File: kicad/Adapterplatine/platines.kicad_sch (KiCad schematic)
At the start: 6 parts, among them X28_1 Conn_01x05_Pin, X29_1 Conn_01x05_Pin, X46 Conn_02x05_Top_Bottom, X46__1 Conn_02x05_Top_Bottom, X48 Conn_02x10_Top_Bottom

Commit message: Bessere Verlegungen Adapterplatine
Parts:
- removed X46, X46__1: Conn_02x05_Top_Bottom, Connector_IDC:IDC-Header_2x05_P2.54mm_Vertical, symbol Connector_Generic:Conn_02x05_Top_Bottom
- added 230V_Platine1, X46: Conn_02x05_Odd_Even, Connector_IDC:IDC-Header_2x05_P2.54mm_Vertical, symbol Connector_Generic:Conn_02x05_Odd_Even
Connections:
- net +5V: now also 230V_Platine1.1 (Pin_1), X46.2 (Pin_2)
- net GND: now also 230V_Platine1.2 (Pin_2), X46.10 (Pin_10)
- new net: 230V_Platine1.10 (Pin_10), X46.1 (Pin_1)
- new net: 230V_Platine1.3 (Pin_3), X46.9 (Pin_9)
- new net: 230V_Platine1.4 (Pin_4), X46.8 (Pin_8)
- new net: 230V_Platine1.5 (Pin_5), X46.7 (Pin_7)
- new net: 230V_Platine1.6 (Pin_6), X46.6 (Pin_6)
- new net: 230V_Platine1.7 (Pin_7), X46.5 (Pin_5)
- new net: 230V_Platine1.8 (Pin_8), X46.4 (Pin_4)
- new net: 230V_Platine1.9 (Pin_9), X46.3 (Pin_3)

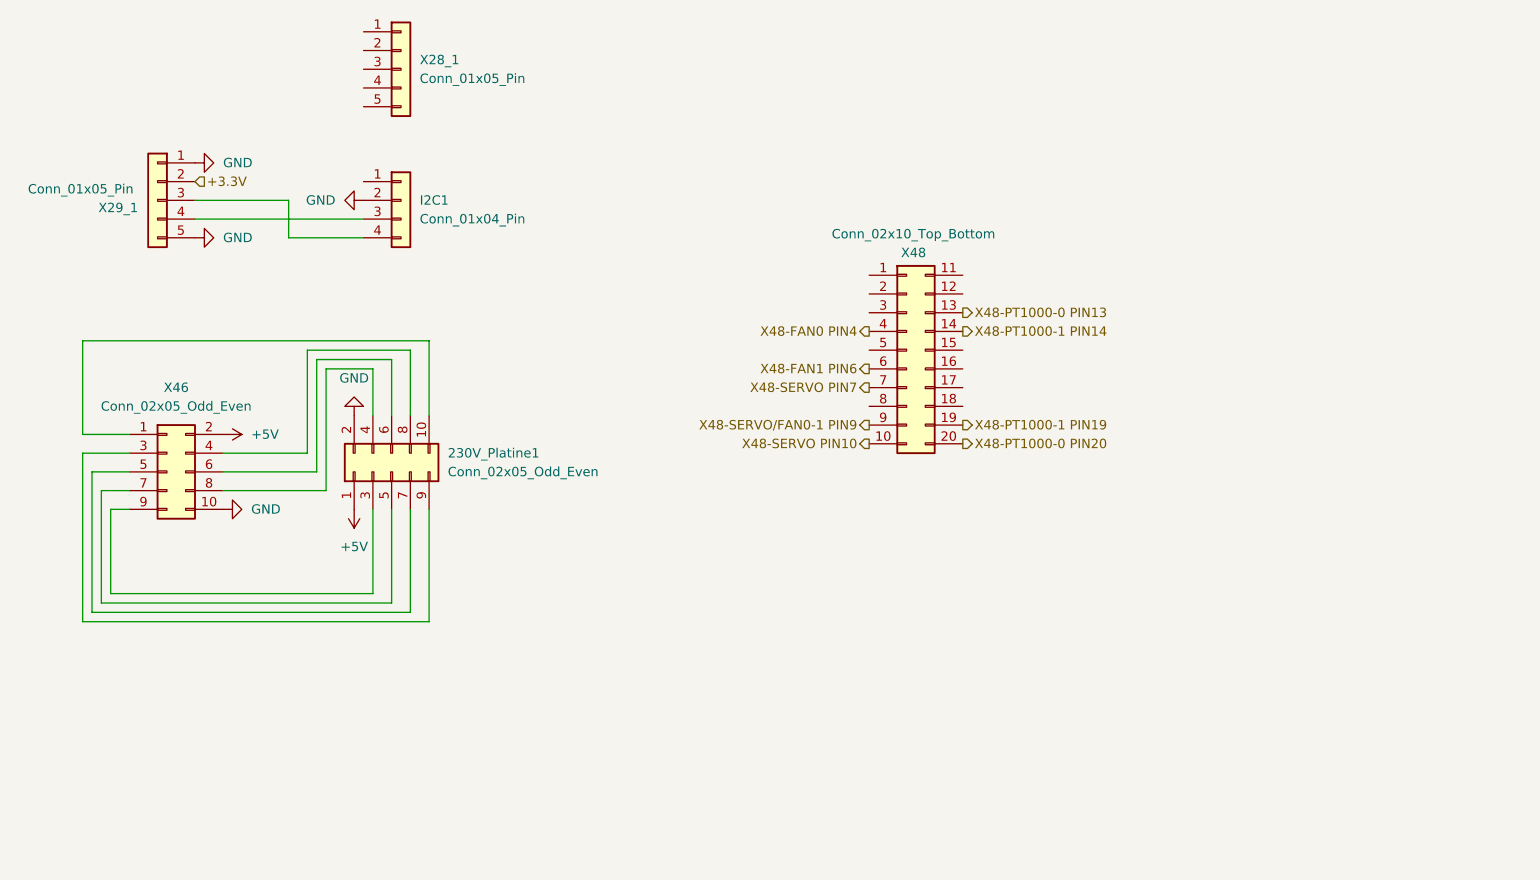
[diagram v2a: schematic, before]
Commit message: Abschlussbericht angefangen/ Adapterplatine ECR DCR
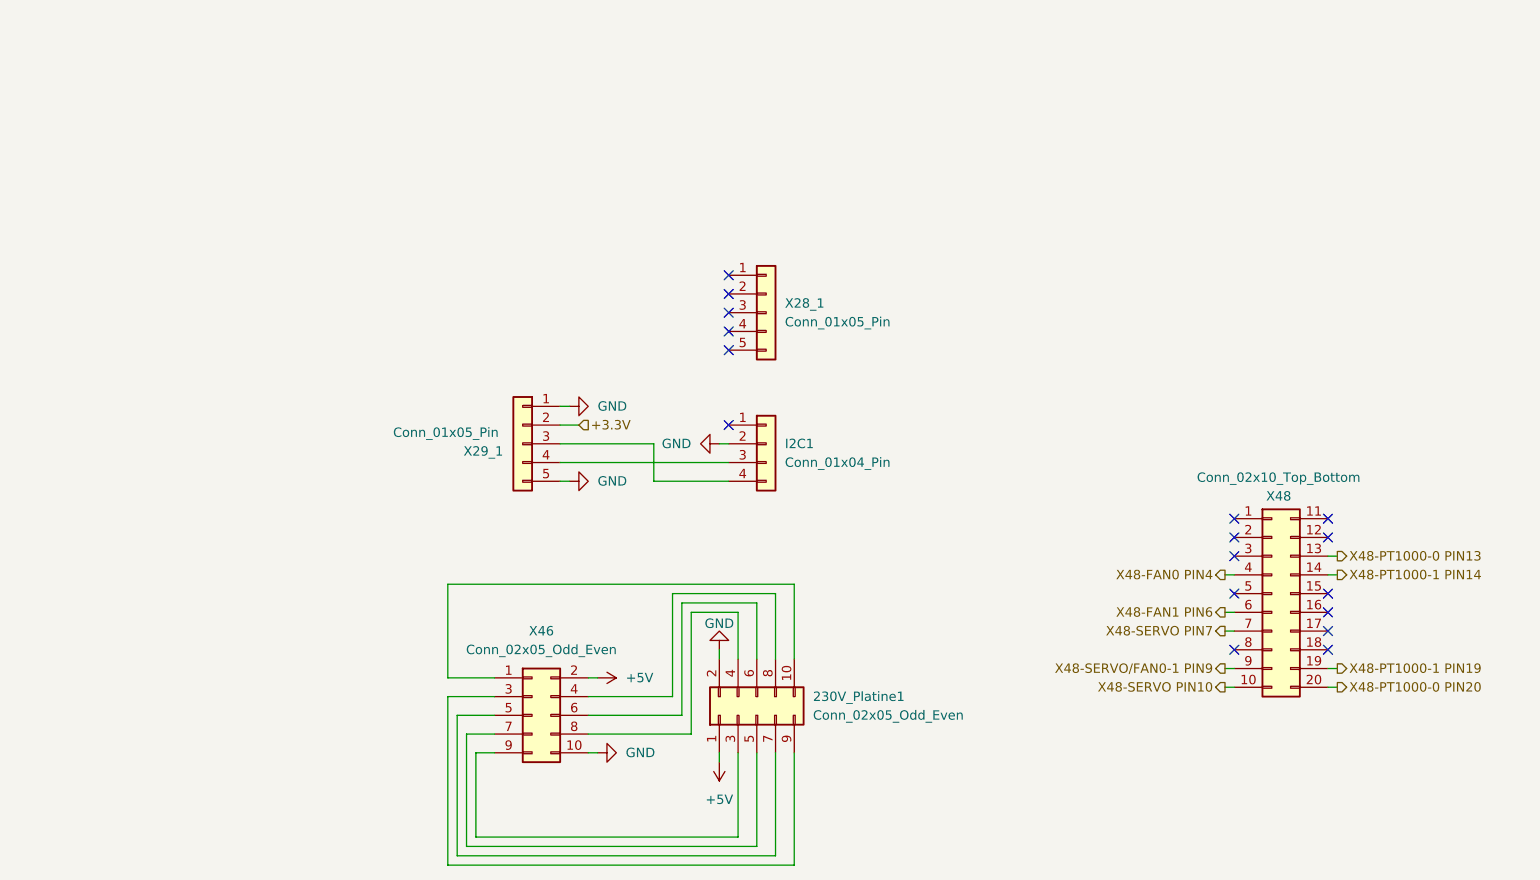
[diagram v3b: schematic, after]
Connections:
- no-connect marks 0 -> 17
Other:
- moved on the sheet: 230V_Platine1, I2C1, X28_1, X29_1, X46, X48

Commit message: i2c Steuerung Filament Fertig
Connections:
- net +5V: now also 230V_Platine1.10 (Pin_10), X46.9 (Pin_9); no longer 230V_Platine1.1 (Pin_1), X46.2 (Pin_2)
- net GND: now also 230V_Platine1.9 (Pin_9), X46.1 (Pin_1); no longer 230V_Platine1.2 (Pin_2), X46.10 (Pin_10)
- net at 230V_Platine1.3 (Pin_3): now also X46.7 (Pin_7); no longer X46.9 (Pin_9)
- net at X46.8 (Pin_8): now also 230V_Platine1.2 (Pin_2); no longer 230V_Platine1.4 (Pin_4)
- net at 230V_Platine1.5 (Pin_5): now also X46.5 (Pin_5); no longer X46.7 (Pin_7)
- net at X46.6 (Pin_6): now also 230V_Platine1.4 (Pin_4); no longer 230V_Platine1.6 (Pin_6)
- net at 230V_Platine1.7 (Pin_7): now also X46.3 (Pin_3); no longer X46.5 (Pin_5)
- net at X46.4 (Pin_4): now also 230V_Platine1.6 (Pin_6); no longer 230V_Platine1.8 (Pin_8)
- new net: 230V_Platine1.1 (Pin_1), X46.10 (Pin_10)
- new net: 230V_Platine1.8 (Pin_8), X46.2 (Pin_2)
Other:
- moved on the sheet: 230V_Platine1, X46
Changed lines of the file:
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@@
-	(wire
-		(pts
-			(xy 129.54 130.81) (xy 129.54 116.84)
-		)
-		(stroke
-			(width 0)
-			(type default)
-		)
-	)
 	(wire
 		(pts
@@
 	(wire
 		(pts
+			(xy 124.46 116.84) (xy 124.46 128.27)
+		)
+		(stroke
+			(width 0)
+			(type default)
+		)
+	)
+	(wire
+		(pts
 			(xy 121.92 74.93) (xy 123.19 74.93)
 		)
@@
 	(wire
 		(pts
-			(xy 132.08 132.08) (xy 132.08 116.84)
+			(xy 132.08 116.84) (xy 132.08 132.08)
+		)
+		(stroke
+			(width 0)
+			(type default)
+		)
+	)
+	(wire
+		(pts
+			(xy 129.54 116.84) (xy 129.54 130.81)
 		)
 		(stroke
@@
 	(wire
 		(pts
-			(xy 127 129.54) (xy 127 116.84)
+			(xy 127 116.84) (xy 127 129.54)
 		)
 		(stroke
@@
 		(pts
 			(xy 115.57 95.25) (xy 115.57 109.22)
-		)
-		(stroke
-			(width 0)
-			(type default)
-		)
-	)
-	(wire
-		(pts
-			(xy 124.46 116.84) (xy 124.46 128.27)
 		)
 		(stroke
@@
 	(symbol
 		(lib_id "Connector_Generic:Conn_02x05_Odd_Even")
-		(at 127 111.76 90)
+		(at 127 109.22 270)
 		(unit 1)
 		(body_style 1)
@@
 					(size 1.27 1.27)
 				)
-				(justify right)
+				(justify left)
 			)
 		)
@@
 					(size 1.27 1.27)
 				)
-				(justify right)
+				(justify left)
 			)
 		)
 		(property "Footprint" "Connector_IDC:IDC-Header_2x05_P2.54mm_Vertical"
-			(at 127 111.76 0)
+			(at 127 109.22 0)
 			(hide yes)
 			(show_name no)
@@
 		)
 		(property "Datasheet" ""
-			(at 127 111.76 0)
+			(at 127 109.22 0)
 			(hide yes)
 			(show_name no)
@@
 		)
 		(property "Description" "Generic connector, double row, 02x05, odd/even pin numbering scheme (row 1 odd numbers, row 2 even numbers), script generated (kicad-library-utils/schlib/autogen/connector/)"
-			(at 127 111.76 0)
+			(at 127 109.22 0)
 			(hide yes)
 			(show_name no)
@@
 		)
 		(property "Hersteller" ""
-			(at 127 111.76 0)
+			(at 127 109.22 0)
 			(hide yes)
 			(show_name no)
@@
 		)
 		(property "Herstellerbezeichnung" ""
-			(at 127 111.76 0)
+			(at 127 109.22 0)
 			(hide yes)
 			(show_name no)
@@
 		)
 		(property "Alternative" ""
-			(at 127 111.76 0)
+			(at 127 109.22 0)
 			(hide yes)
 			(show_name no)
@@
 	(symbol
 		(lib_id "Connector_Generic:Conn_02x05_Odd_Even")
-		(at 96.52 111.76 0)
+		(at 99.06 111.76 180)
 		(unit 1)
 		(body_style 1)
@@
 		)
 		(property "Footprint" "Connector_IDC:IDC-Header_2x05_P2.54mm_Vertical"
-			(at 96.52 111.76 0)
+			(at 99.06 111.76 0)
 			(hide yes)
 			(show_name no)
@@
 		)
 		(property "Datasheet" ""
-			(at 96.52 111.76 0)
+			(at 99.06 111.76 0)
 			(hide yes)
 			(show_name no)
@@
 		)
 		(property "Description" "Generic connector, double row, 02x05, odd/even pin numbering scheme (row 1 odd numbers, row 2 even numbers), script generated (kicad-library-utils/schlib/autogen/connector/)"
-			(at 96.52 111.76 0)
+			(at 99.06 111.76 0)
 			(hide yes)
 			(show_name no)
@@
 		)
 		(property "Hersteller" ""
-			(at 96.52 111.76 0)
+			(at 99.06 111.76 0)
 			(hide yes)
 			(show_name no)
@@
 		)
 		(property "Herstellerbezeichnung" ""
-			(at 96.52 111.76 0)
+			(at 99.06 111.76 0)
 			(hide yes)
 			(show_name no)
@@
 		)
 		(property "Alternative" ""
-			(at 96.52 111.76 0)
-			(hide yes)
-			(show_name no)
+			(at 99.06 111.76 0)
+			(hide yes)
+			(show_name no)

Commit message: Adapterplatine Version 1.0 final
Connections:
- net X48-FAN0 PIN4: now also X48.14 (Pin_14); no longer X48.4 (Pin_4)
- net X48-FAN1 PIN6: now also X48.16 (Pin_16); no longer X48.6 (Pin_6)
- net X48-PT1000-0 PIN13: now also X48.3 (Pin_3); no longer X48.13 (Pin_13)
- net X48-PT1000-0 PIN20: now also X48.10 (Pin_10); no longer X48.20 (Pin_20)
- net X48-PT1000-1 PIN14: now also X48.4 (Pin_4); no longer X48.14 (Pin_14)
- net X48-PT1000-1 PIN19: now also X48.9 (Pin_9); no longer X48.19 (Pin_19)
- net X48-SERVO PIN10: now also X48.20 (Pin_20); no longer X48.10 (Pin_10)
- net X48-SERVO PIN7: now also X48.17 (Pin_17); no longer X48.7 (Pin_7)
- net X48-SERVO/FAN0-1 PIN9: now also X48.19 (Pin_19); no longer X48.9 (Pin_9)
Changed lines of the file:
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@@
 	(symbol
 		(lib_id "Connector_Generic:Conn_02x10_Top_Bottom")
-		(at 196.85 95.25 0)
+		(at 199.39 95.25 0)
+		(mirror y)
 		(unit 1)
 		(body_style 1)
@@
 		(dnp no)
 		(property "Reference" "X48"
-			(at 196.088 82.042 0)
+			(at 200.152 82.042 0)
 			(show_name no)
 			(do_not_autoplace no)
@@
 		)
 		(property "Value" "Conn_02x10_Top_Bottom"
-			(at 186.69 79.502 0)
+			(at 209.55 79.502 0)
 			(show_name no)
 			(do_not_autoplace no)
@@
 		)
 		(property "Footprint" "Connector_Molex:Molex_Mini-Fit_Jr_5566-20A_2x10_P4.20mm_Vertical"
-			(at 196.85 95.25 0)
+			(at 199.39 95.25 0)
 			(hide yes)
 			(show_name no)
@@
 		)
 		(property "Datasheet" ""
-			(at 196.85 95.25 0)
+			(at 199.39 95.25 0)
 			(hide yes)
 			(show_name no)
@@
 		)
 		(property "Description" "Generic connector, double row, 02x10, top/bottom pin numbering scheme (row 1: 1...pins_per_row, row2: pins_per_row+1 ... num_pins), script generated (kicad-library-utils/schlib/autogen/connector/)"
-			(at 196.85 95.25 0)
+			(at 199.39 95.25 0)
 			(hide yes)
 			(show_name no)
@@
 		)
 		(property "Hersteller" ""
-			(at 196.85 95.25 0)
+			(at 199.39 95.25 0)
 			(hide yes)
 			(show_name no)
@@
 		)
 		(property "Herstellerbezeichnung" ""
-			(at 196.85 95.25 0)
+			(at 199.39 95.25 0)
 			(hide yes)
 			(show_name no)
@@
 		)
 		(property "Alternative" ""
-			(at 196.85 95.25 0)
+			(at 199.39 95.25 0)
 			(hide yes)
 			(show_name no)
